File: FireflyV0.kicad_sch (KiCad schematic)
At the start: 15 parts, among them J1 USB4125-GF-A-0190, J2 USB4125-GF-A-0190, U1 Pico, U2 LEDS4, U3 LEDS4, U4 LEDS4, U5 LEDS4

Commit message: Done minus accelerometer
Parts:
- removed R1, R2: R_US, Resistor_SMD:R_0805_2012Metric, symbol Device:R_US
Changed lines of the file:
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@@
 (kicad_sch (version 20211123) (generator eeschema)
   (paper "A4")
-  (junction (at 104.14 146.05) (diameter 0) (color 0 0 0 0)
-  )
-  (junction (at 143.51 146.05) (diameter 0) (color 0 0 0 0)
-  )
   (junction (at 227.33 138.43) (diameter 0) (color 0 0 0 0)
   )
@@
     (stroke (width 0) (type default) (color 0 0 0 0))
   )
-  (wire (pts (xy 104.14 146.05) (xy 105.41 146.05))
-    (stroke (width 0) (type default) (color 0 0 0 0))
-  )
-  (wire (pts (xy 143.51 144.78) (xy 143.51 146.05))
-    (stroke (width 0) (type default) (color 0 0 0 0))
-  )
   (wire (pts (xy 241.3 30.48) (xy 243.84 30.48))
     (stroke (width 0) (type default) (color 0 0 0 0))
@@
     (stroke (width 0) (type default) (color 0 0 0 0))
   )
-  (wire (pts (xy 102.87 146.05) (xy 104.14 146.05))
-    (stroke (width 0) (type default) (color 0 0 0 0))
-  )
-  (wire (pts (xy 143.51 146.05) (xy 144.78 146.05))
+  (wire (pts (xy 102.87 146.05) (xy 105.41 146.05))
     (stroke (width 0) (type default) (color 0 0 0 0))
   )
@@
     (stroke (width 0) (type default) (color 0 0 0 0))
   )
-  (wire (pts (xy 104.14 144.78) (xy 104.14 146.05))
-    (stroke (width 0) (type default) (color 0 0 0 0))
-  )
-  (wire (pts (xy 142.24 146.05) (xy 143.51 146.05))
+  (wire (pts (xy 142.24 146.05) (xy 144.78 146.05))
     (stroke (width 0) (type default) (color 0 0 0 0))
   )
@@
     )
   )
-  (global_label "3V3" (shape input) (at 143.51 137.16 90) (fields_autoplaced)
-    (effects (font (size 1.27 1.27)) (justify left))
-    (property "Intersheet References" "${INTERSHEET_REFS}" (id 0) (at 143.4306 131.2393 90)
-      (effects (font (size 1.27 1.27)) (justify left) hide)
-    )
-  )
   (global_label "LED_DATA_3" (shape input) (at 123.19 106.68 180) (fields_autoplaced)
     (effects (font (size 1.27 1.27)) (justify right))
@@
     (property "Intersheet References" "${INTERSHEET_REFS}" (id 0) (at 228.7269 32.9406 0)
       (effects (font (size 1.27 1.27)) (justify right) hide)
-    )
-  )
-  (global_label "3V3" (shape input) (at 104.14 137.16 90) (fields_autoplaced)
-    (effects (font (size 1.27 1.27)) (justify left))
-    (property "Intersheet References" "${INTERSHEET_REFS}" (id 0) (at 104.0606 131.2393 90)
-      (effects (font (size 1.27 1.27)) (justify left) hide)
     )
   )
@@
     (pin "2")
     (pin "3")
-  )
-  (symbol (lib_id "Device:R_US") (at 104.14 140.97 0) (unit 1)
-    (in_bom yes) (on_board yes) (fields_autoplaced)
-    (property "Reference" "R1" (id 0) (at 106.68 139.6999 0)
-      (effects (font (size 1.27 1.27)) (justify left))
-    )
-    (property "Value" "R_US" (id 1) (at 106.68 142.2399 0)
-      (effects (font (size 1.27 1.27)) (justify left))
-    )
-    (property "Footprint" "Resistor_SMD:R_0805_2012Metric" (id 2) (at 105.156 141.224 90)
-      (effects (font (size 1.27 1.27)) hide)
-    )
-    (property "Datasheet" "~" (id 3) (at 104.14 140.97 0)
-      (effects (font (size 1.27 1.27)) hide)
-    )
-    (pin "1")
-    (pin "2")
   )
   (symbol (lib_id "SamacSys_Parts:EVQ-P7J01P") (at 105.41 146.05 0) (unit 1)
@@
     (pin "3")
     (pin "4")
-  )
-  (symbol (lib_id "Device:R_US") (at 143.51 140.97 0) (unit 1)
-    (in_bom yes) (on_board yes) (fields_autoplaced)
-    (property "Reference" "R2" (id 0) (at 146.05 139.6999 0)
-      (effects (font (size 1.27 1.27)) (justify left))
-    )
-    (property "Value" "R_US" (id 1) (at 146.05 142.2399 0)
-      (effects (font (size 1.27 1.27)) (justify left))
-    )
-    (property "Footprint" "Resistor_SMD:R_0805_2012Metric" (id 2) (at 144.526 141.224 90)
-      (effects (font (size 1.27 1.27)) hide)
-    )
-    (property "Datasheet" "~" (id 3) (at 143.51 140.97 0)
-      (effects (font (size 1.27 1.27)) hide)
-    )
-    (pin "1")
-    (pin "2")
   )
   (symbol (lib_id "SamacSys_Parts:EVQ-P7J01P") (at 144.78 146.05 0) (unit 1)
@@
       (reference "MK1") (unit 1) (value "CMM-4737DT-26186-TR") (footprint "SamacSys_Parts:CMM4737DT26186TR")
     )
-    (path "/24b16c5b-0018-45db-b224-2842c6e2e903"
-      (reference "R1") (unit 1) (value "R_US") (footprint "Resistor_SMD:R_0805_2012Metric")
-    )
-    (path "/96b72fe4-573a-4b34-b6b6-1d56716b11b9"
-      (reference "R2") (unit 1) (value "R_US") (footprint "Resistor_SMD:R_0805_2012Metric")
-    )
     (path "/219f344c-be83-4066-9867-bc2789be2025"

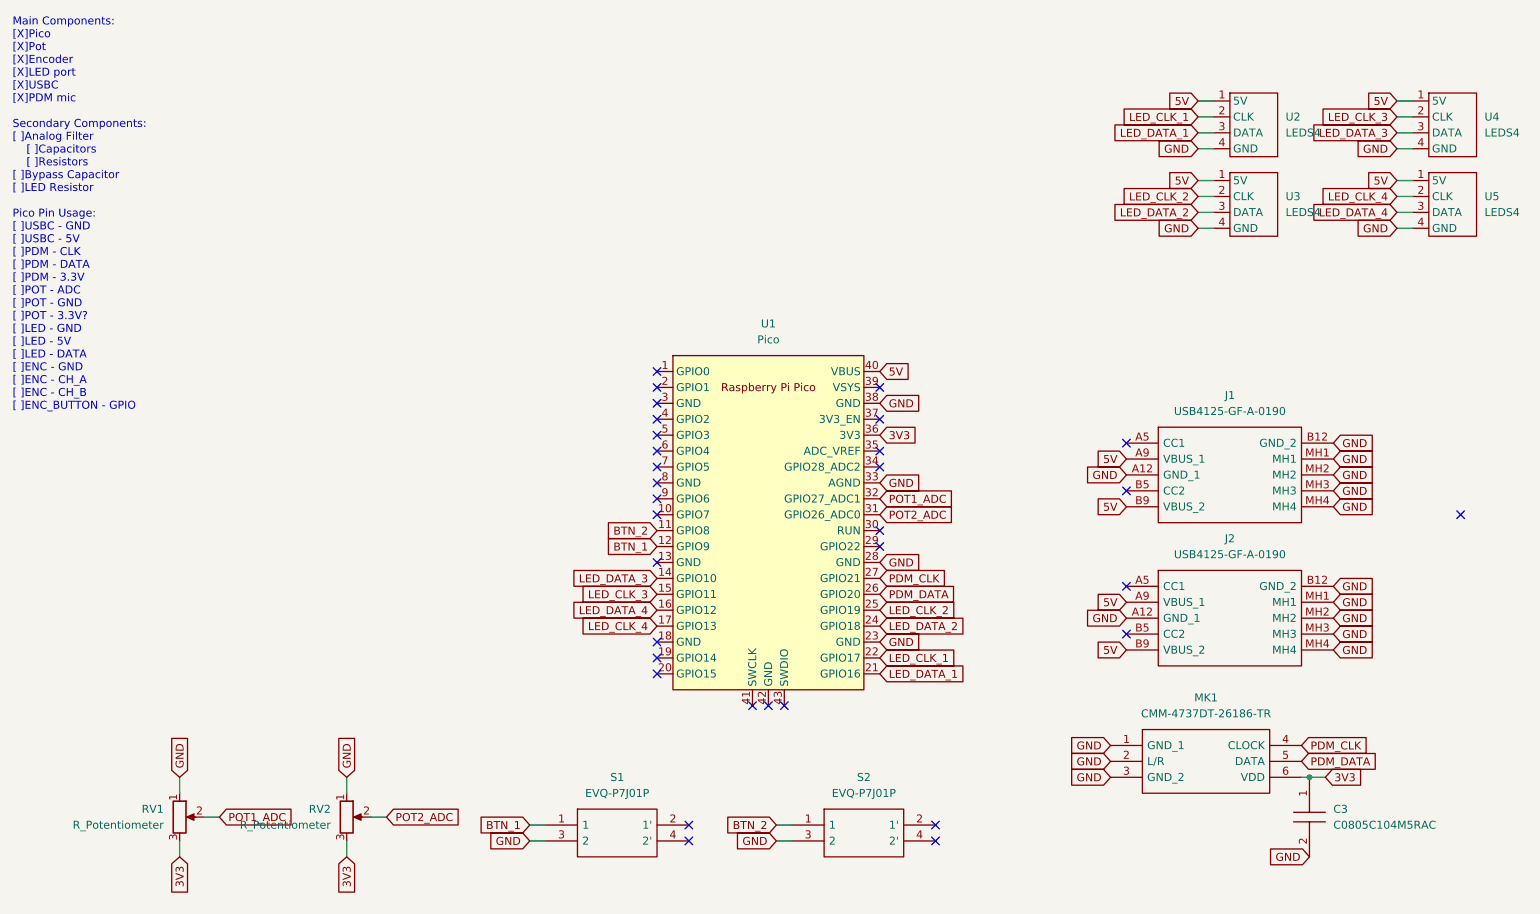
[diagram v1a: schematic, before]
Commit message: Adding bom, switching switch
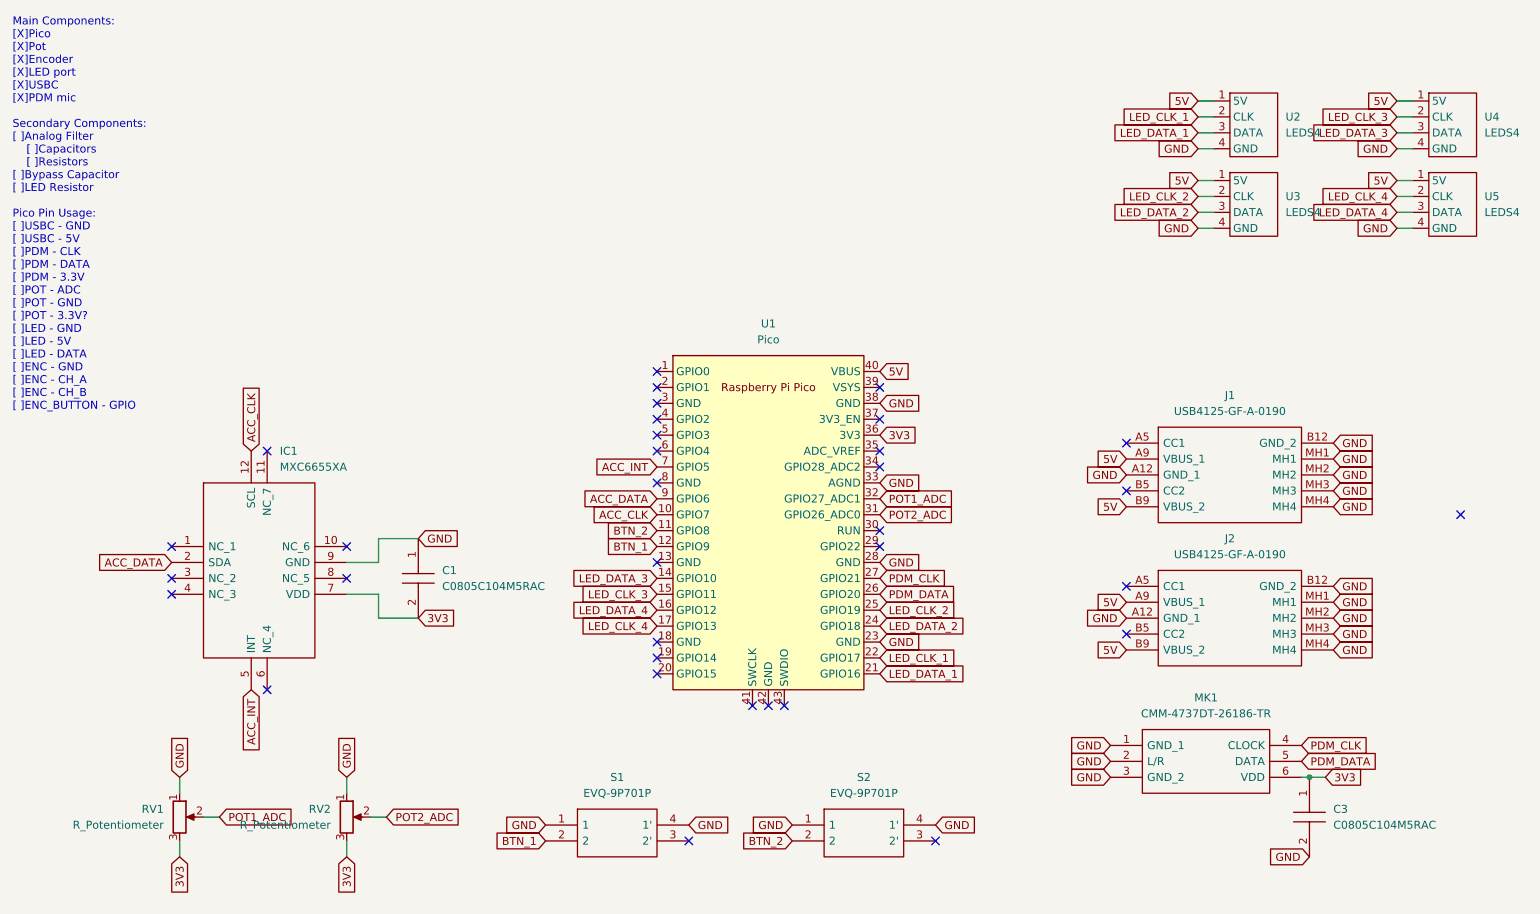
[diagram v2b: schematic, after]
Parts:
- removed S1, S2: EVQ-P7J01P, EVQP7J01P, symbol SamacSys_Parts:EVQ-P7J01P
- added C1: C0805C104M5RAC, Capacitor_SMD:C_0805_2012Metric, symbol SamacSys_Parts:C0805C104M5RAC
- added IC1: MXC6655XA, MXC6655XA, symbol SamacSys_Parts:MXC6655XA
- added S1, S2: EVQ-9P701P, EVQ-9P701P, symbol SamacSys_Parts:EVQ-9P701P
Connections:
- net 3V3: now also C1.2, IC1.7 (VDD)
- net BTN_1: now also S1.2
- net BTN_2: now also S2.2
- net GND: now also C1.1, IC1.9 (GND), S1.1, S1.4 (1'), S2.1, S2.4 (1')
- net ACC_CLK: now reaches U1.10 (GPIO7)
- net ACC_CLK: now also IC1.12 (SCL)
- net ACC_INT: now reaches U1.7 (GPIO5)
- net ACC_INT: now also IC1.5 (INT)
- net ACC_DATA: now reaches U1.9 (GPIO6)
- net ACC_DATA: now also IC1.2 (SDA)
- no-connect marks 32 -> 34

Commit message: Uploading ordered rev1 files
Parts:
- added R1, R2, R3, R4: R_US, Resistor_SMD:R_0805_2012Metric, symbol Device:R_US
- C1: footprint Capacitor_SMD:C_0805_2012Metric -> CAPC2012X88N
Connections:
- net 3V3: now also C1.1; no longer C1.2
- net GND: now also C1.2, R1.1, R2.1, R3.1, R4.1; no longer C1.1
- net at J2.A5 (CC1): now also R3.2
- net at J2.B5 (CC2): now also R4.2
- net at J1.A5 (CC1): now also R1.2
- net at J1.B5 (CC2): now also R2.2
- no-connect marks 34 -> 30
